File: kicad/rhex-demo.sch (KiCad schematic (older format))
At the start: 24 parts

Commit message: main thread for testing
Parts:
- added HC-06?: HC-06-bluetooth, symbol HC-06-bluetooth
- gave numbers to parts that had none: 6
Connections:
- net at M1.1 (PWM): now also C7.1, R1.1
- net +6V: now reaches M1.2 (+)
- net +6V: now also C1.1, C2.1, C3.1, C4.1, C5.1, C6.1, M2.2 (+), M3.2 (+), M4.2 (+), M5.2 (+), M6.2 (+)
- net GND: now reaches M1.3 (-)
- net GND: now also C1.2, C2.2, C3.2, C4.2, C5.2, C6.2, M2.3 (-), M3.3 (-), M4.3 (-), M5.3 (-), M6.3 (-)
- net at M2.1 (PWM): now also C8.1, R2.1
- net at M3.1 (PWM): now also C9.1, R3.1
- net at M4.1 (PWM): now also C10.1, R4.1
- net at M5.1 (PWM): now also C11.1, R5.1
- net at M6.1 (PWM): now also C12.1, R6.1
- net PWM1: now reaches R1.2
- net PWM2: now reaches R2.2
- net PWM3: now reaches R3.2
- net PWM4: now reaches R4.2
- net PWM5: now reaches R5.2
- net PWM6: now reaches R6.2
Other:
- moved on the sheet: C1, C10, C11, C12, C2, C3, C4, C5, C6, C7, C8, C9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

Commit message: layout half done
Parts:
- removed C2, C3, C4, C5: 470uF, symbol C
- removed HC-06?: HC-06-bluetooth, symbol HC-06-bluetooth
- removed R3, R4, R5, R6: 10kR, symbol R
- added C13, C16, C18: 100pF, Capacitors_THT:C_Axial_L3.8mm_D2.6mm_P7.50mm_Horizontal, symbol C
- added C14: 10uF, Capacitors_THT:C_Axial_L3.8mm_D2.6mm_P7.50mm_Horizontal, symbol C
- added C15, C17: 100nF, Capacitors_THT:C_Axial_L3.8mm_D2.6mm_P7.50mm_Horizontal, symbol C
- added DCDC1: DCDC-6010-M, rhex:DCDC-6010-M, symbol DCDC-6010-M
- added DSN-1504-3A1: DCDC2, rhex2:DSN-1504-2A1, symbol DSN-1504-3A
- added HAL1, HAL10, HAL11, HAL12, HAL2, HAL3, HAL4, HAL5, HAL6, HAL7, HAL8, HAL9: TLE4905L, Pin_Headers:Pin_Header_Straight_1x03_Pitch2.54mm, symbol TLE4905L
- added HC-6: HC-06-bluetooth, Pin_Headers:Pin_Header_Straight_1x06_Pitch2.54mm, symbol HC-06-bluetooth
- added J1: MCU power, Pin_Headers:Pin_Header_Straight_1x02_Pitch2.54mm, symbol Conn_01x02
- added PA3, PA6, PA7, PB0, PB13, PB9, PC1, PC2, PC3, PC6, PC7, PD12, PD13, PD14, PD2, PD3, PE0, PE15, PE2, PE6: GPIO_PIN, Pin_Headers:Pin_Header_Straight_1x01_Pitch2.54mm, symbol GPIO_PIN
- C1, C11, C6, C9: footprint (none) -> Capacitors_THT:C_Axial_L3.8mm_D2.6mm_P7.50mm_Horizontal
- C10: value 10uF -> 100pF; footprint (none) -> Capacitors_THT:C_Axial_L3.8mm_D2.6mm_P7.50mm_Horizontal
- C12, C8: value 10uF -> 100nF; footprint (none) -> Capacitors_THT:C_Axial_L3.8mm_D2.6mm_P7.50mm_Horizontal
- C7: value 10nF -> 10uF; footprint (none) -> Capacitors_THT:C_Axial_L3.8mm_D2.6mm_P7.50mm_Horizontal
- M1, M2, M3, M4, M5, M6: footprint (none) -> Pin_Headers:Pin_Header_Straight_1x03_Pitch2.54mm
- R1: value 10kR -> 10k; footprint (none) -> Resistors_THT:R_Axial_DIN0204_L3.6mm_D1.6mm_P5.08mm_Horizontal
- R2: value 10kR -> 20k; footprint (none) -> Resistors_THT:R_Axial_DIN0204_L3.6mm_D1.6mm_P5.08mm_Horizontal
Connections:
- net +6V is gone; now on an unnamed net: C1.1, C6.1, M1.2 (+), M2.2 (+), M3.2 (+), M4.2 (+), M5.2 (+), M6.2 (+)
- net GND: now also C11.2, C12.2, R2.1, C13.2, C14.2, C15.2, C16.2, DCDC1.4 (OUT-), DSN-1504-3A1.4 (Out-), HAL1.2 (GND), HAL10.2 (GND), HAL11.2 (GND), HAL12.2 (GND), HAL2.2 (GND), HAL3.2 (GND), HAL4.2 (GND), HAL5.2 (GND), HAL6.2 (GND), HAL7.2 (GND), HAL8.2 (GND), HAL9.2 (GND), HC-6.~ (VDD), J1.2 (Pin_2)
- net at M3.1 (PWM): now also PB0.~; no longer C9.1
- net at M4.1 (PWM): now also PD12.~; no longer C10.1
- net at C11.1: now also C12.1, C13.1, DCDC1.3 (OUT+); no longer M5.1 (PWM)
- net at M6.1 (PWM): now also PD14.~; no longer C12.1
- net -BATT: now reaches C8.2
- net -BATT: now also C10.2, C7.2, C9.2, C17.2, C18.2, DCDC1.2 (IN-), DSN-1504-3A1.2 (In-)
- net PWM1: no longer names the net of R1.2
- net PWM1: now also PC6.~
- net PWM2: no longer names the net of R2.2
- net PWM2: now also R1.1, HC-6.~ (VDD)
- new net: M1.1 (PWM), PA6.~
- new net: M2.1 (PWM), PA7.~
- new net: M5.1 (PWM), PD13.~
- new net: C14.1, C15.1, C16.1, DSN-1504-3A1.3 (Out+), HAL1.1 (Vs), HAL10.1 (Vs), HAL11.1 (Vs), HAL12.1 (Vs), HAL2.1 (Vs), HAL3.1 (Vs), HAL4.1 (Vs), HAL5.1 (Vs), HAL6.1 (Vs), HAL7.1 (Vs), HAL8.1 (Vs), HAL9.1 (Vs), HC-6.~ (VDD), J1.1 (Pin_1)
- new net: HAL1.3 (Q), PE2.~
- new net: HAL3.3 (Q), PC1.~
- new net: HAL5.3 (Q), PC3.~
- new net: HAL7.3 (Q), PE15.~
- new net: HAL9.3 (Q), PD2.~
- new net: HAL11.3 (Q), PB9.~
- new net: HAL2.3 (Q), PE6.~
- new net: HAL4.3 (Q), PC2.~
- new net: HAL6.3 (Q), PA3.~
- new net: HAL8.3 (Q), PB13.~
- new net: HAL10.3 (Q), PD3.~
- new net: HAL12.3 (Q), PE0.~
- new net: HC-6.~ (VDD), PC7.~
- new net +BATT: C10.1, C17.1, C18.1, C7.1, C8.1, C9.1, DCDC1.1 (IN+), DSN-1504-3A1.1 (In+)
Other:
- note added: "Application shield for STM32F4 Discovery to connect servo motors, hal sensors,\nand a bluetooth module."
- note added: "Spybot Rhex application shield for STM32F4 Discovery"
- moved on the sheet: C1, C6

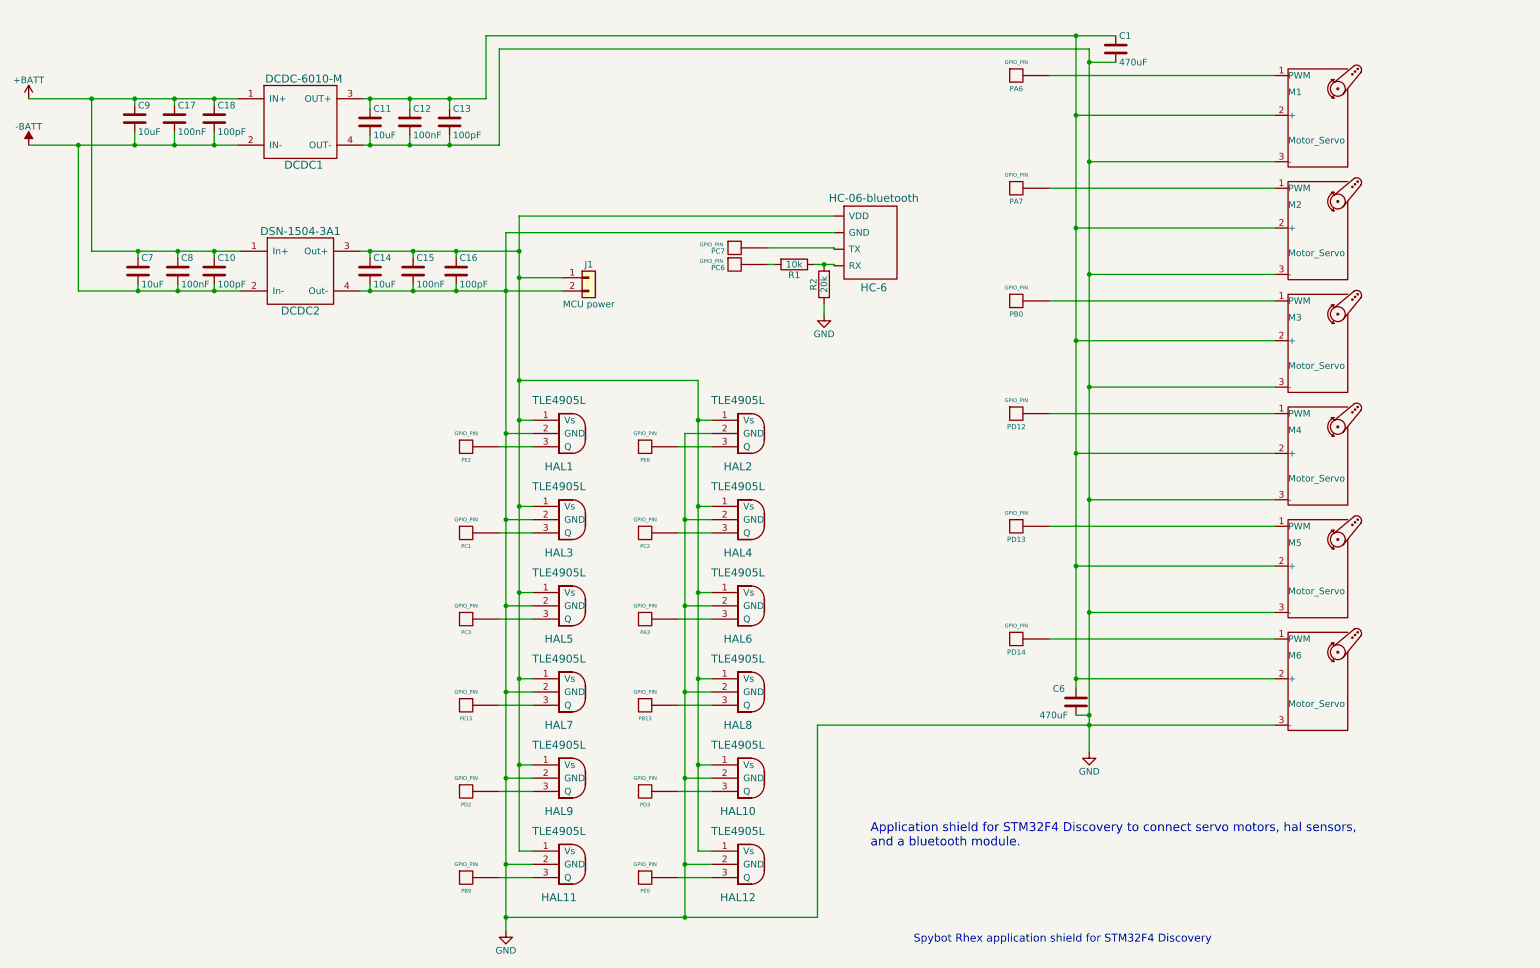
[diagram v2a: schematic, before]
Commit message: pcb layout done, generated gerb files, generated report files
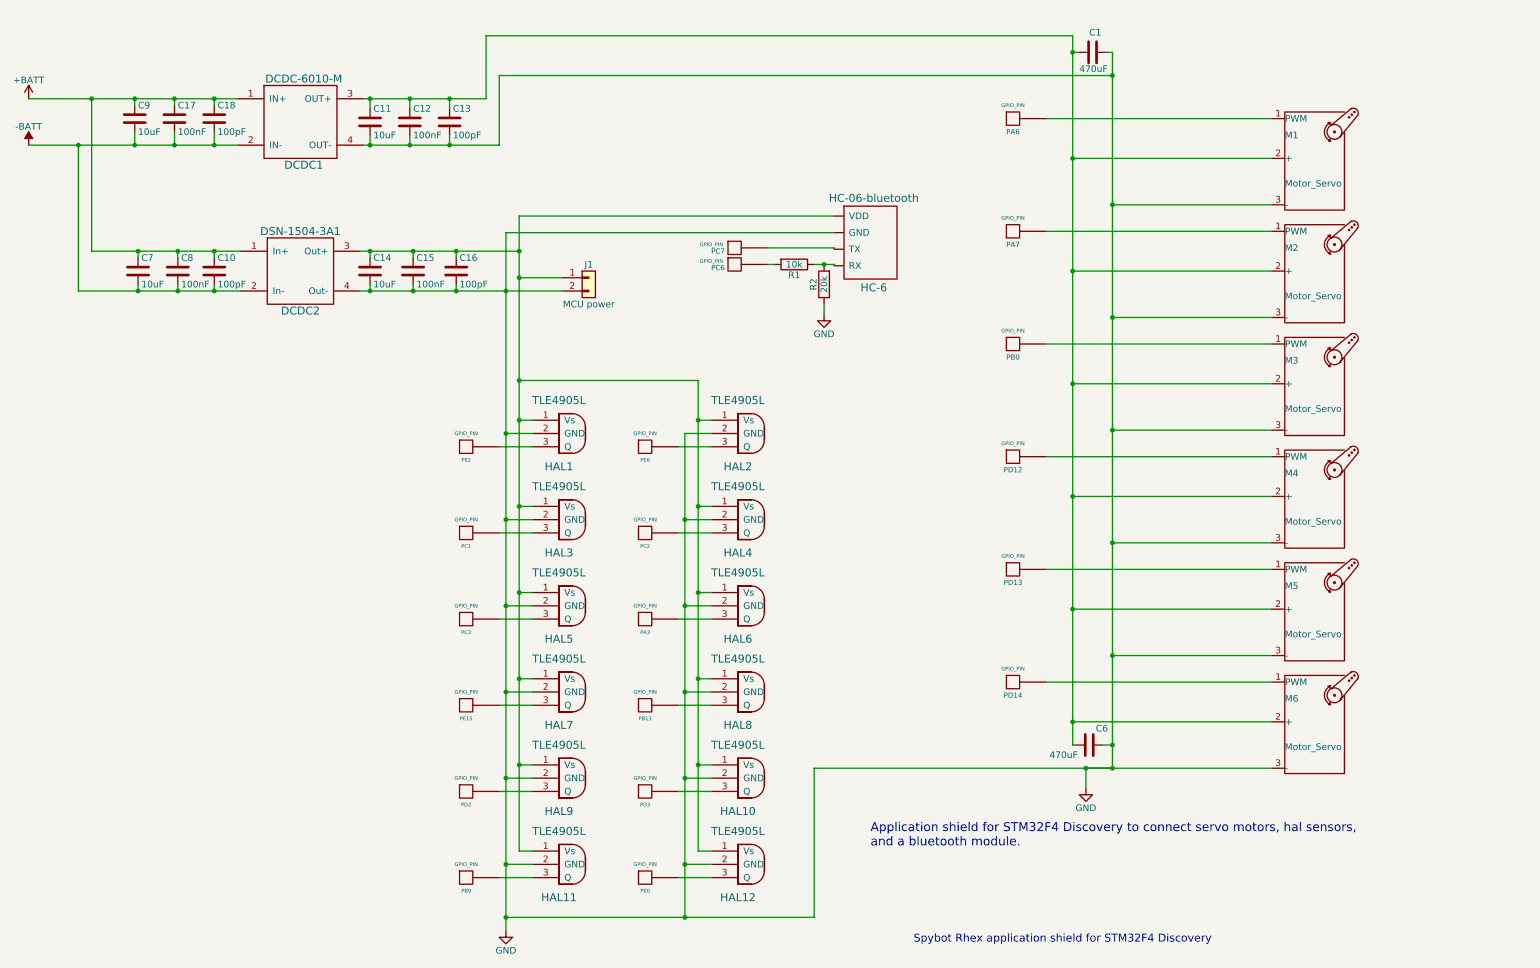
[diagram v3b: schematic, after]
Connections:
- net GND: now also C1.1, C6.1; no longer C1.2, C6.2
- net at C11.1, C12.1, C13.1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: now also C1.2, C6.2; no longer C1.1, C6.1
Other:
- moved on the sheet: C1, C6, M1, M2, M3, M4, M5, M6, PA6, PA7, PB0, PD12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

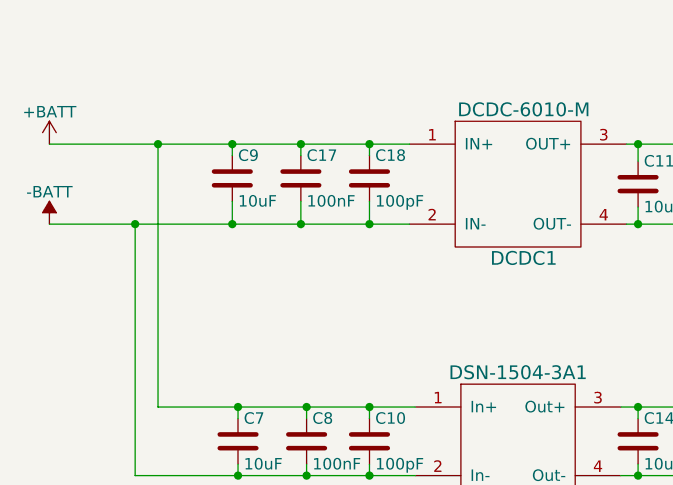
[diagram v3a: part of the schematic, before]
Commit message: minor changes to layout design, regenerated prints, changed sclk to 100MHz
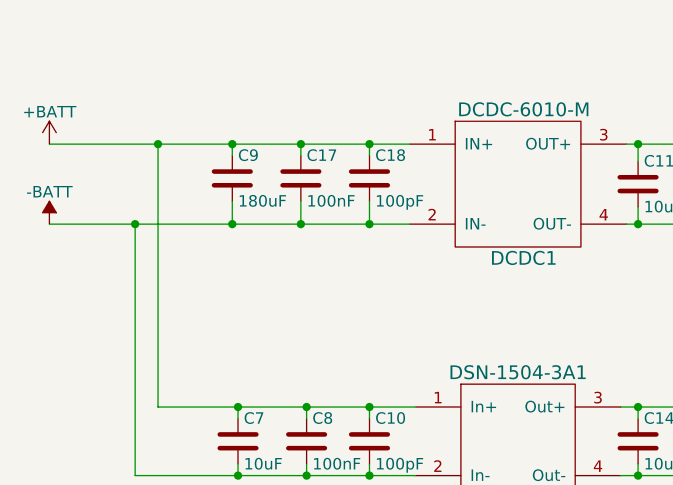
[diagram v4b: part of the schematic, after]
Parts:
- C9: value 10uF -> 180uF
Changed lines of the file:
@@
 P 1500 1275
 F 0 "C9" H 1525 1375 50  0000 L CNN
-F 1 "10uF" H 1525 1175 50  0000 L CNN
+F 1 "180uF" H 1525 1175 50  0000 L CNN
 F 2 "Capacitors_THT:C_Axial_L3.8mm_D2.6mm_P7.50mm_Horizontal" H 1538 1125 50  0001 C CNN
 F 3 "" H 1500 1275 50  0001 C CNN

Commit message: add leg detection functions
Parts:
- HC-6: footprint Pin_Headers:Pin_Header_Straight_1x06_Pitch2.54mm -> Socket_Strips:Socket_Strip_Straight_1x06_Pitch2.54mm
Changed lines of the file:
@@
 F 0 "HC-6" H 7075 1850 60  0000 C CNN
 F 1 "HC-06-bluetooth" H 7075 2525 60  0000 C CNN
-F 2 "Pin_Headers:Pin_Header_Straight_1x06_Pitch2.54mm" H 7075 2140 60  0001 C CNN
+F 2 "Socket_Strips:Socket_Strip_Straight_1x06_Pitch2.54mm" H 7075 2140 60  0001 C CNN
 F 3 "" H 7075 2140 60  0001 C CNN
 	1    7025 2200
